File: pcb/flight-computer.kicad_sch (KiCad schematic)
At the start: 46 parts, among them J1 MicroSD Slot, J2 USB_C_Receptacle_USB2.0_16P, SW1 SW_Push, SW2 SW_Push, U1 RP2040, U2 W25Q16JVSS, U3 USBLC6-2SC6, Y1 12MHz

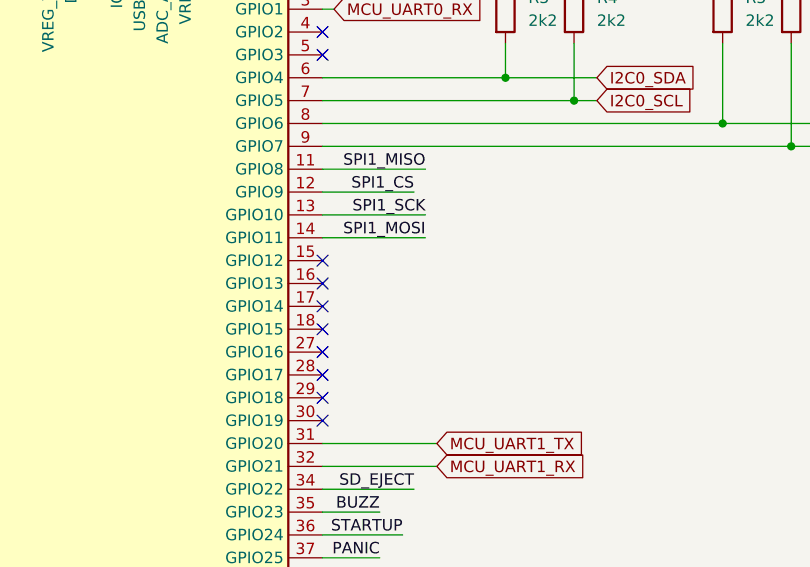
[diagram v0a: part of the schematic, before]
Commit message: Added interrupt lines for IMU and magnetometer
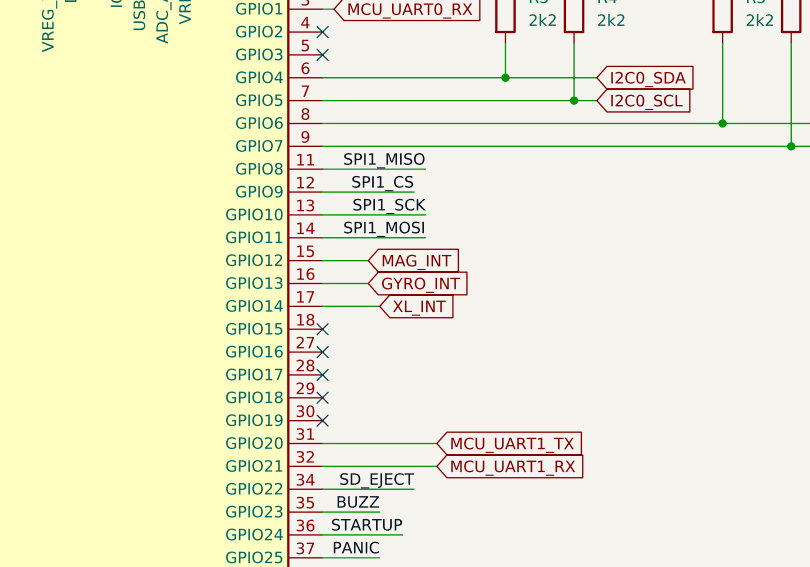
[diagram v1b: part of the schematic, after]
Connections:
- net MAG_INT: now reaches U1.15 (GPIO12)
- net GYRO_INT: now reaches U1.16 (GPIO13)
- net XL_INT: now reaches U1.17 (GPIO14)
- no-connect marks 19 -> 16
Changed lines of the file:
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@@
-	)
-	(no_connect
-		(at 222.25 83.82)
 	)
 	(no_connect
@@
 	)
 	(no_connect
-		(at 222.25 88.9)
-	)
-	(no_connect
 		(at 222.25 60.96)
 	)
@@
 	)
 	(no_connect
-		(at 222.25 86.36)
-	)
-	(no_connect
 		(at 45.72 232.41)
 	)
@@
 	(wire
 		(pts
+			(xy 227.33 86.36) (xy 222.25 86.36)
+		)
+		(stroke
+			(width 0)
+			(type default)
+		)
+	)
+	(wire
+		(pts
 			(xy 242.57 63.5) (xy 222.25 63.5)
 		)
@@
 	(wire
 		(pts
+			(xy 222.25 88.9) (xy 228.6 88.9)
+		)
+		(stroke
+			(width 0)
+			(type default)
+		)
+	)
+	(wire
+		(pts
 			(xy 161.29 176.53) (xy 172.72 176.53)
 		)
@@
 		(pts
 			(xy 199.39 45.72) (xy 201.93 45.72)
+		)
+		(stroke
+			(width 0)
+			(type default)
+		)
+	)
+	(wire
+		(pts
+			(xy 227.33 83.82) (xy 222.25 83.82)
 		)
 		(stroke
@@
 			)
 			(justify right bottom)
+		)
+	)
+	(global_label "GYRO_INT"
+		(shape input)
+		(at 227.33 86.36 0)
+		(fields_autoplaced yes)
+		(effects
+			(font
+				(size 1.27 1.27)
+			)
+			(justify left)
+		)
+		(property "Intersheetrefs" "${INTERSHEET_REFS}"
+			(at 239.1448 86.36 0)
+			(effects
+				(font
+					(size 1.27 1.27)
+				)
+				(justify left)
+				(hide yes)
+			)
 		)
 	)
@@
 			(effects
 				(font
+					(size 1.27 1.27)
+				)
+				(justify left)
+				(hide yes)
+			)
+		)
+	)
+	(global_label "MAG_INT"
+		(shape input)
+		(at 227.33 83.82 0)
+		(fields_autoplaced yes)
+		(effects
+			(font
+				(size 1.27 1.27)
+			)
+			(justify left)
+		)
+		(property "Intersheetrefs" "${INTERSHEET_REFS}"
+			(at 237.9957 83.82 0)
+			(effects
+				(font
+					(size 1.27 1.27)
+				)
+				(justify left)
+				(hide yes)
+			)
+		)
+	)
+	(global_label "XL_INT"
+		(shape input)
+		(at 228.6 88.9 0)
+		(fields_autoplaced yes)
+		(effects
+			(font
+				(size 1.27 1.27)
+			)
+			(justify left)
+		)
+		(property "Intersheetrefs" "${INTERSHEET_REFS}"
+			(at 237.6933 88.9 0)
+			(effects
+				(font

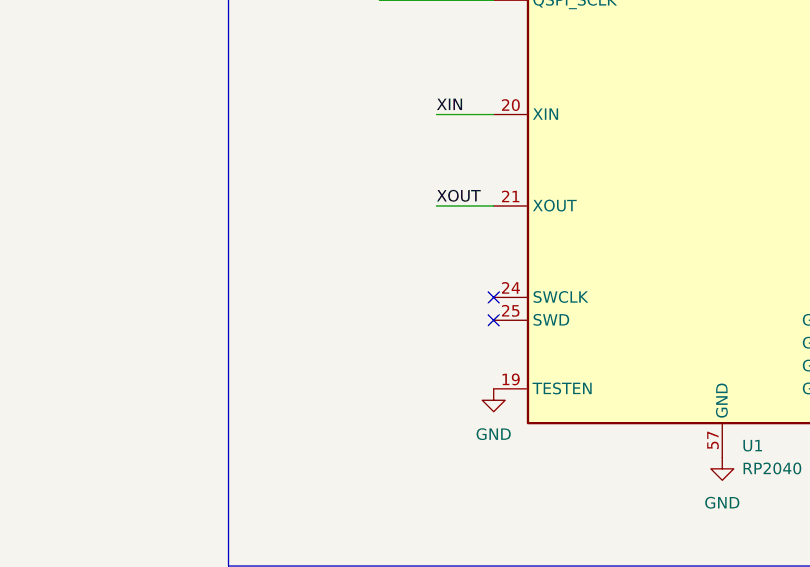
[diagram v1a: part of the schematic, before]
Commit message: Revamping docs, added SWD test pads.
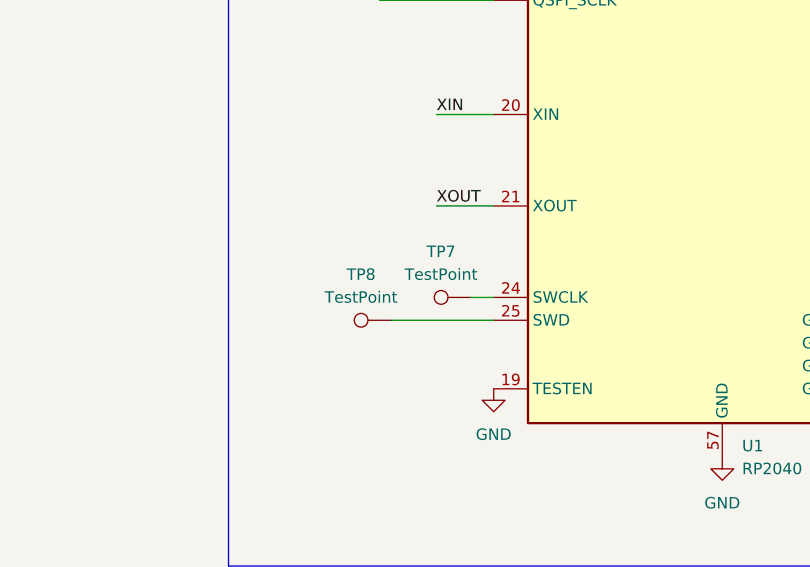
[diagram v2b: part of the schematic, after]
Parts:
- added TP7, TP8: TestPoint, TestPoint:TestPoint_Pad_D1.5mm, symbol Connector:TestPoint
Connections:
- net at U1.24 (SWCLK): now also TP7.1
- net at U1.25 (SWD): now also TP8.1
- no-connect marks 16 -> 14
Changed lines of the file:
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@@
 	)
 	(no_connect
-		(at 171.45 121.92)
-	)
-	(no_connect
 		(at 222.25 96.52)
 	)
@@
 	)
 	(no_connect
-		(at 171.45 119.38)
-	)
-	(no_connect
 		(at 45.72 232.41)
 	)
@@
 	(wire
 		(pts
+			(xy 160.02 121.92) (xy 171.45 121.92)
+		)
+		(stroke
+			(width 0)
+			(type default)
+		)
+	)
+	(wire
+		(pts
 			(xy 195.58 176.53) (xy 207.01 176.53)
 		)
@@
 	(wire
 		(pts
+			(xy 168.91 119.38) (xy 171.45 119.38)
+		)
+		(stroke
+			(width 0)
+			(type default)
+		)
+	)
+	(wire
+		(pts
 			(xy 222.25 88.9) (xy 228.6 88.9)
 		)
@@
 	)
 	(symbol
+		(lib_id "Connector:TestPoint")
+		(at 168.91 119.38 90)
+		(unit 1)
+		(exclude_from_sim no)
+		(in_bom yes)
+		(on_board yes)
+		(dnp no)
+		(fields_autoplaced yes)
+		(property "Reference" "TP7"
+			(at 165.608 114.3 90)
+			(effects
+				(font
+					(size 1.27 1.27)
+				)
+			)
+		)
+		(property "Value" "TestPoint"
+			(at 165.608 116.84 90)
+			(effects
+				(font
+					(size 1.27 1.27)
+				)
+			)
+		)
+		(property "Footprint" "TestPoint:TestPoint_Pad_D1.5mm"
+			(at 168.91 114.3 0)
+			(effects
+				(font
+					(size 1.27 1.27)
+				)
+				(hide yes)
+			)
+		)
+		(property "Datasheet" "~"
+			(at 168.91 114.3 0)
+			(effects
+				(font
+					(size 1.27 1.27)
+				)
+				(hide yes)
+			)
+		)
+		(property "Description" "test point"
+			(at 168.91 119.38 0)
+			(effects
+				(font
+					(size 1.27 1.27)
+				)
+				(hide yes)
+			)
+		)
+		(pin "1"
+		)
+		(instances
+			(project "flight-computer"
+				(path "/b90d3133-97a4-4747-8a68-e80f353c7b97"
+					(reference "TP7")
+					(unit 1)
+				)
+			)
+		)
+	)
+	(symbol
 		(lib_id "Device:C")
 		(at 85.09 129.54 0)
@@
 					(unit 1)
 				)
+			)
+		)
+	)
+	(symbol
+		(lib_id "Connector:TestPoint")
+		(at 160.02 121.92 90)
+		(unit 1)
+		(exclude_from_sim no)
+		(in_bom yes)
+		(on_board yes)
+		(dnp no)
+		(fields_autoplaced yes)
+		(property "Reference" "TP8"
+			(at 156.718 116.84 90)
+			(effects
+				(font
+					(size 1.27 1.27)
+				)
+			)
+		)
+		(property "Value" "TestPoint"
+			(at 156.718 119.38 90)
+			(effects
+				(font
+					(size 1.27 1.27)
+				)
+			)
+		)
+		(property "Footprint" "TestPoint:TestPoint_Pad_D1.5mm"
+			(at 160.02 116.84 0)
+			(effects
+				(font
+					(size 1.27 1.27)
+				)
+				(hide yes)
+			)
+		)
+		(property "Datasheet" "~"
+			(at 160.02 116.84 0)
+			(effects
+				(font
+					(size 1.27 1.27)
+				)
+				(hide yes)
+			)
+		)
+		(property "Description" "test point"
+			(at 160.02 121.92 0)
+			(effects
+				(font
+					(size 1.27 1.27)
+				)
+				(hide yes)
+			)
+		)
+		(pin "1"
+		)
+		(instances
+			(project "flight-computer"
+				(path "/b90d3133-97a4-4747-8a68-e80f353c7b97"
+					(reference "TP8")
+					(unit 1)
+				)

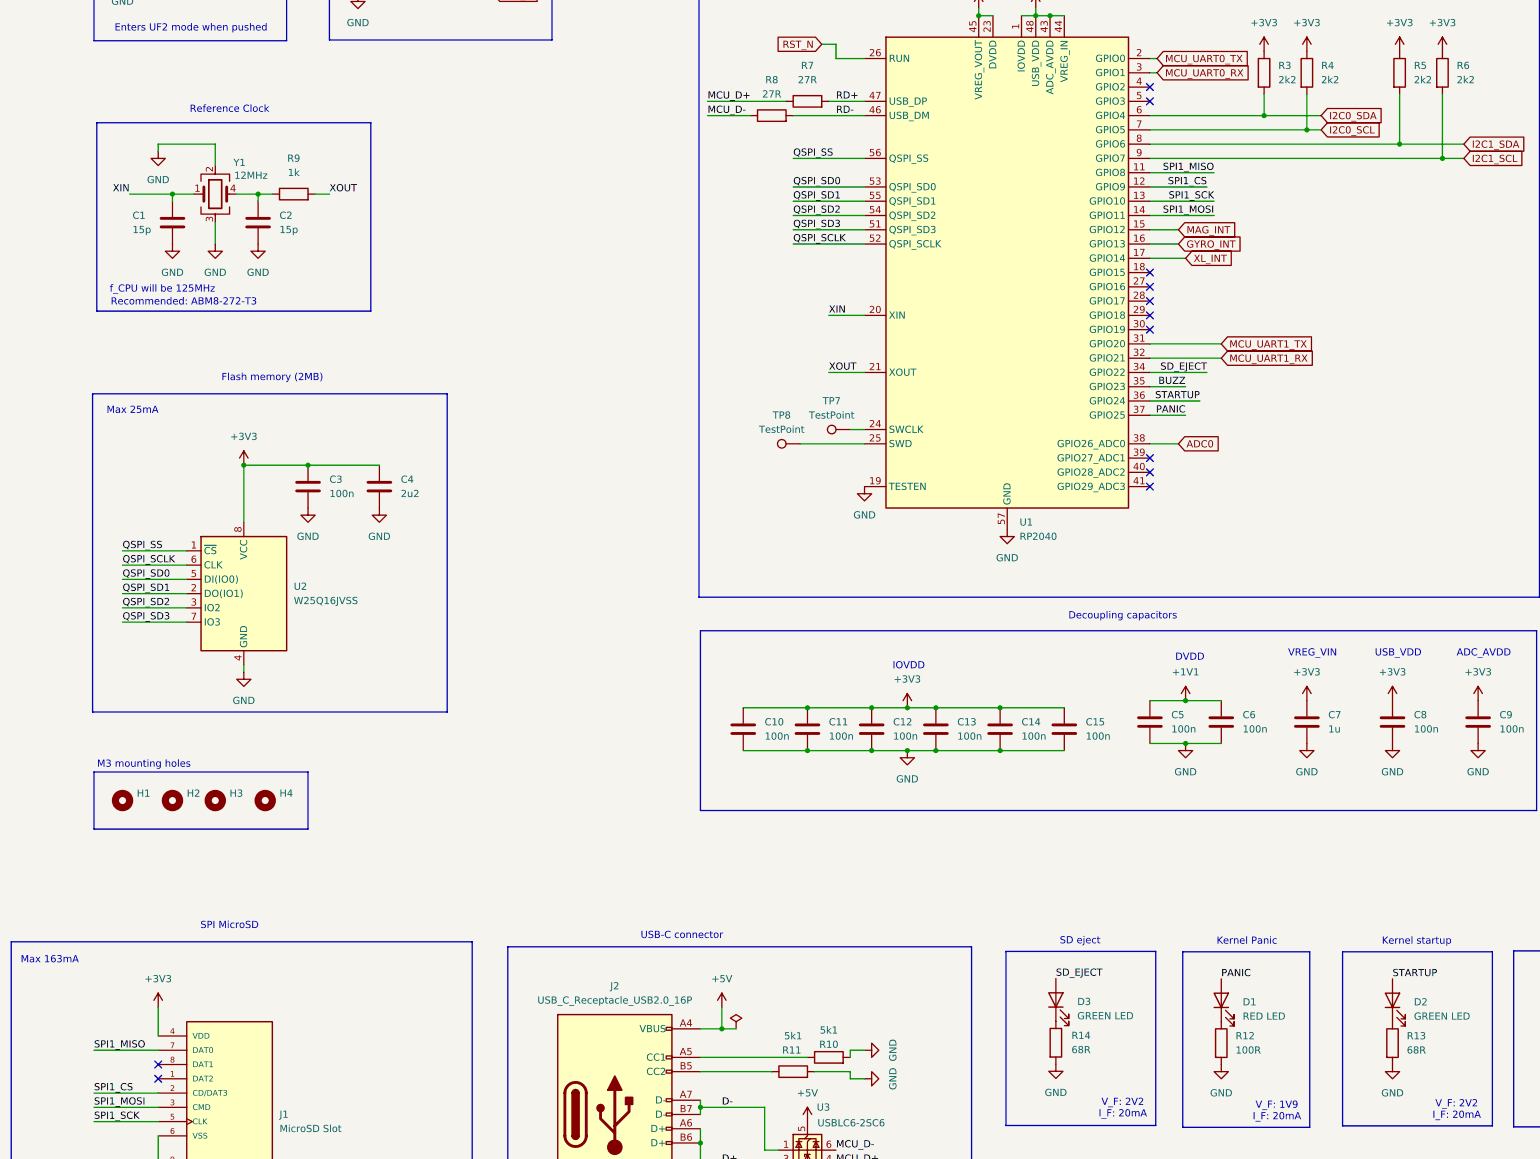
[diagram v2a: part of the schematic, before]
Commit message: Changed LED resistors to 330 ohms to reduce brightness.
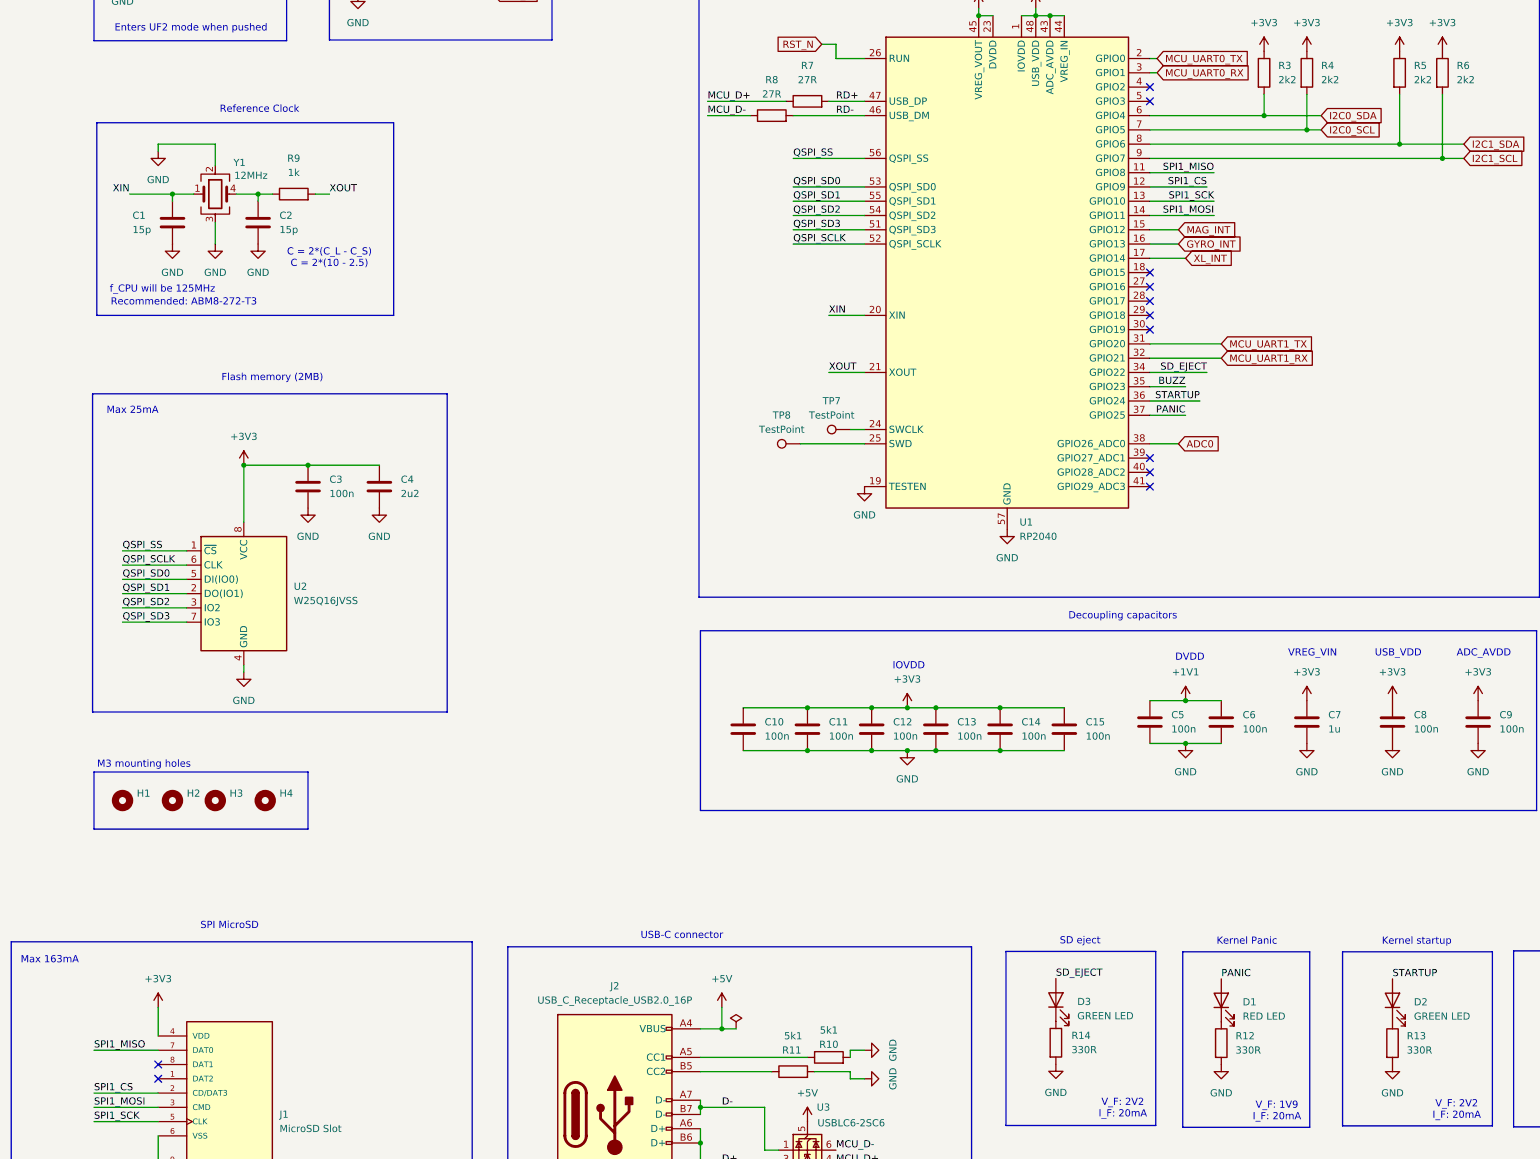
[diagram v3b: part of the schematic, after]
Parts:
- R12: value 100R -> 330R; MP ERJ-U02J101X -> 560112110231
- R13, R14: value 68R -> 330R; MP ERA-2AED680X -> 560112110231
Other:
- note added: "C = 2*(C_L - C_S) C = 2*(10 - 2.5)"
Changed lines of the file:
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@@
 	(rectangle
 		(start 34.798 64.77)
-		(end 83.566 98.298)
+		(end 87.63 99.06)
 		(stroke
 			(width 0)
@@
 		)
 	)
+	(text "C = 2*(C_L - C_S)\nC = 2*(10 - 2.5)"
+		(exclude_from_sim no)
+		(at 76.2 88.9 0)
+		(effects
+			(font
+				(size 1.27 1.27)
+			)
+		)
+	)
 	(text "Kernel Panic"
 		(exclude_from_sim no)
@@
 	(text "Reference Clock"
 		(exclude_from_sim no)
-		(at 58.42 62.484 0)
+		(at 63.754 62.484 0)
 		(effects
 			(font
@@
 			)
 		)
-		(property "Value" "68R"
+		(property "Value" "330R"
 			(at 208.28 229.8035 0)
 			(effects
@@
 			)
 		)
-		(property "Datasheet" "https://www.mouser.ca/datasheet/2/315/AOA0000C307-1149632.pdf"
+		(property "Datasheet" "https://www.we-online.com/components/products/datasheet/560112110231.pdf"
 			(at 205.508 228.5336 0)
 			(effects
@@
 			)
 		)
-		(property "MP" "ERA-2AED680X"
+		(property "MP" "560112110231"
 			(at 205.508 228.5336 0)
 			(effects
@@
 			)
 		)
-		(property "Value" "68R"
+		(property "Value" "330R"
 			(at 267.97 229.8699 0)
 			(effects
@@
 			)
 		)
-		(property "Datasheet" "https://www.mouser.ca/datasheet/2/315/AOA0000C307-1149632.pdf"
+		(property "Datasheet" "https://www.we-online.com/components/products/datasheet/560112110231.pdf"
 			(at 265.43 228.6 0)
 			(effects
@@
 			)
 		)
-		(property "MP" "ERA-2AED680X"
+		(property "MP" "560112110231"
 			(at 265.43 228.6 0)
 			(effects
@@
 			)
 		)
-		(property "Value" "100R"
+		(property "Value" "330R"
 			(at 237.49 229.8699 0)
 			(effects
@@
 			)
 		)
-		(property "Datasheet" "https://www.mouser.ca/datasheet/2/315/AOA0000C334-1314047.pdf"
+		(property "Datasheet" "https://www.we-online.com/components/products/datasheet/560112110231.pdf"
 			(at 234.95 228.6 0)
 			(effects
@@
 			)
 		)
-		(property "MP" "ERJ-U02J101X"
+		(property "MP" "560112110231"
 			(at 234.95 228.6 0)
 			(effects
